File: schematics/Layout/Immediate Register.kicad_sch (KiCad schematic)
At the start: 3 parts

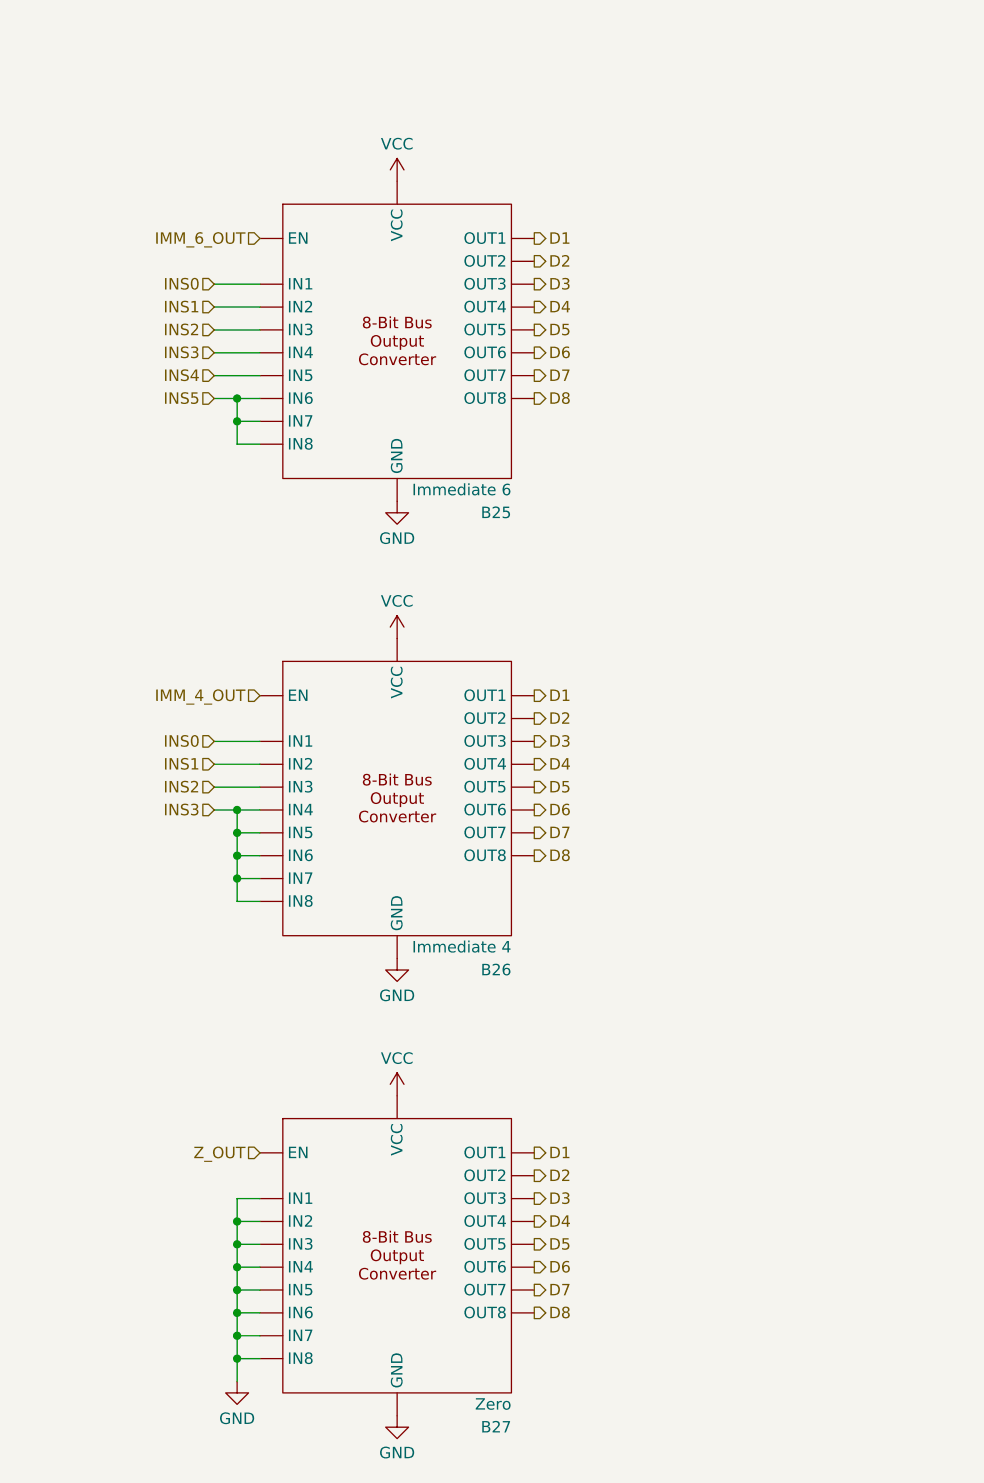
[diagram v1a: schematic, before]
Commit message: Update layout diagram with new boards in following places:  - Added buffer boards to all register boards.  - Fixed PC not getting address lines.  - Added SRAM interface boards.  - Updated to use Mini Control Signals Distributors.
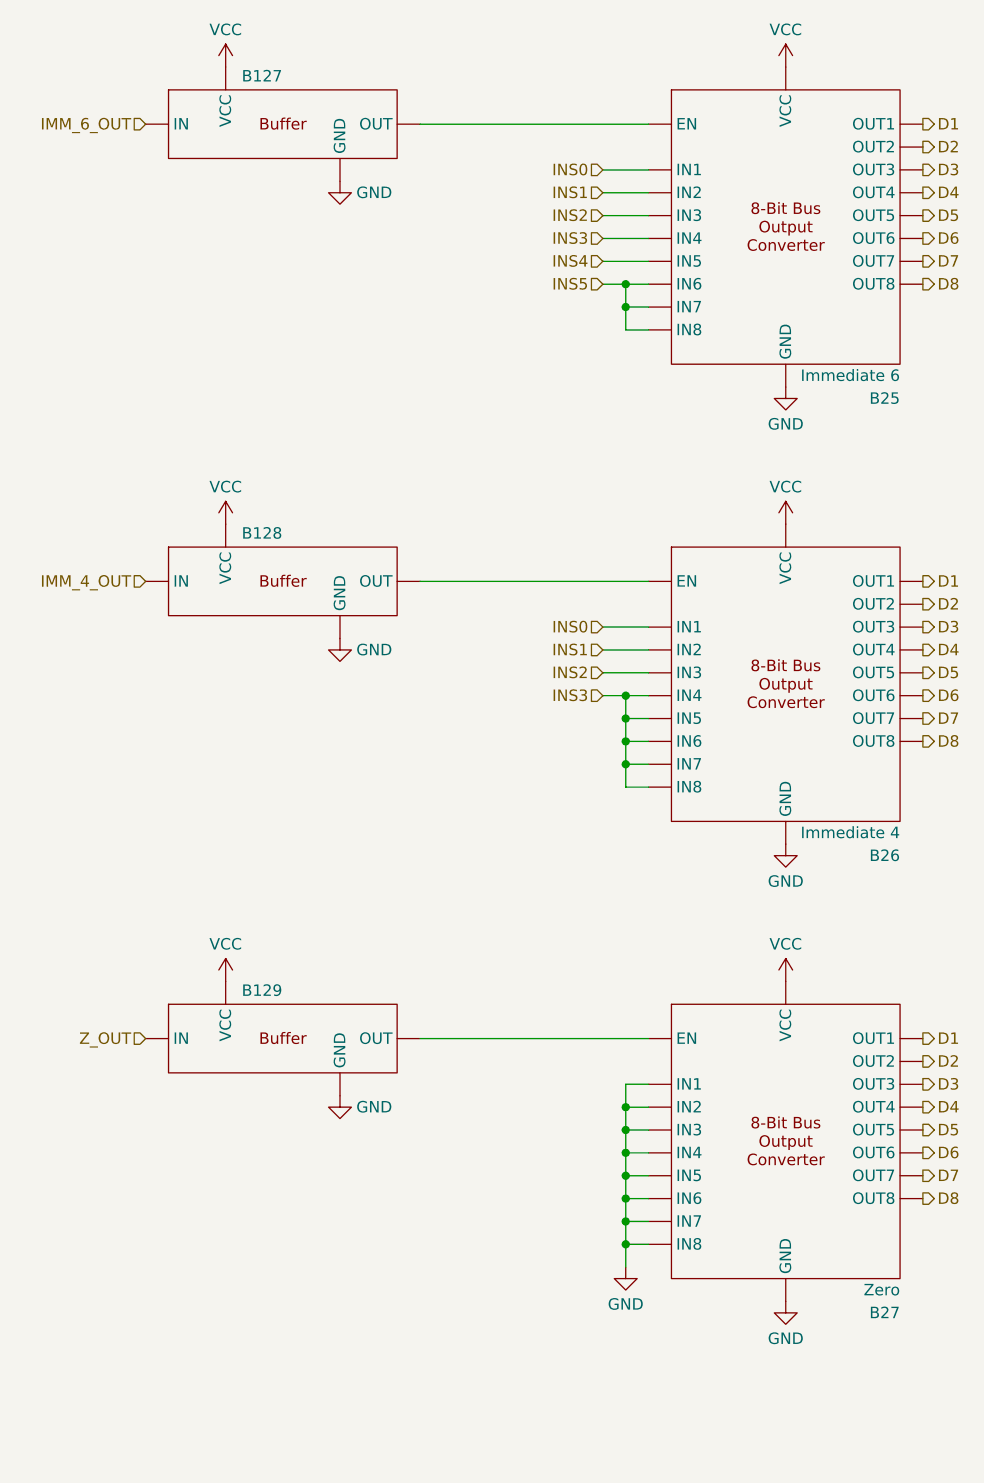
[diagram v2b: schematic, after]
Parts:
- added B127, B128, B129: ~, symbol MiniDragon:Logic Buffer
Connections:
- net GND: now also B127. (OUT), B128. (OUT), B129. (OUT)
- net IMM_4_OUT: now also B128. (OUT); no longer B26. (OUT8)
- net IMM_6_OUT: now also B127. (OUT); no longer B25. (OUT8)
- net VCC: now also B127. (OUT), B128. (OUT), B129. (OUT)
- net Z_OUT: now also B129. (OUT); no longer B27. (OUT8)
- new net: B129. (OUT), B27. (OUT8)
- new net: B127. (OUT), B25. (OUT8)
- new net: B128. (OUT), B26. (OUT8)
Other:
- moved on the sheet: B25, B26, B27

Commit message: Update with new Shift symbol, diagram the rest of the ALU and more instruction decoder boards.
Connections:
- new net: B129. (OUT), B27. (OUT8)
- new net: B127. (OUT), B25. (OUT8)
- new net: B128. (OUT), B26. (OUT8)
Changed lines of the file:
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@@
 	)
 	(symbol
-		(lib_name "Logic Buffer_2")
 		(lib_id "MiniDragon:Logic Buffer")
 		(at 76.2 143.51 0)
@@
 	)
 	(symbol
+		(lib_name "8-bit Bus Output_2")
+		(lib_id "MiniDragon:8-bit Bus Output")
+		(at 132.08 53.34 0)
+		(unit 1)
+		(exclude_from_sim no)
+		(in_bom yes)
+		(on_board yes)
+		(dnp no)
+		(property "Reference" "B25"
+			(at 144.78 72.39 0)
+			(effects
+				(font
+					(size 1.27 1.27)
+				)
+				(justify right)
+			)
+		)
+		(property "Value" "Immediate 6"
+			(at 144.78 69.85 0)
+			(effects
+				(font
+					(size 1.27 1.27)
+				)
+				(justify right)
+			)
+		)
+		(property "Footprint" ""
+			(at 132.08 50.8 0)
+			(effects
+				(font
+					(size 1.27 1.27)
+				)
+				(hide yes)
+			)
+		)
+		(property "Datasheet" ""
+			(at 132.08 50.8 0)
+			(effects
+				(font
+					(size 1.27 1.27)
+				)
+				(hide yes)
+			)
+		)
+		(property "Description" ""
+			(at 132.08 53.34 0)
+			(effects
+				(font
+					(size 1.27 1.27)
+				)
+			)
+		)
+		(pin ""
+		)
+		(pin ""
+		)
+		(pin ""
+		)
+		(pin ""
+		)
+		(pin ""
+		)
+		(pin ""
+		)
+		(pin ""
+		)
+		(pin ""
+		)
+		(pin ""
+		)
+		(pin ""
+		)
+		(pin ""
+		)
+		(pin ""
+		)
+		(pin ""
+		)
+		(pin ""
+		)
+		(pin ""
+		)
+		(pin ""
+		)
+		(pin ""
+		)
+		(pin ""
+		)
+		(pin ""
+		)
+		(instances
+			(project "MiniDragon"
+				(path "/5049efcd-4f75-45d1-9c4f-a0a8d8f08d5b/22b03389-15d6-4e58-ab5f-e64946b54731"
+					(reference "B25")
+					(unit 1)
+				)
+			)
+		)
+	)
+	(symbol
+		(lib_name "Logic Buffer_2")
+		(lib_id "MiniDragon:Logic Buffer")
+		(at 76.2 41.91 0)
+		(unit 1)
+		(exclude_from_sim no)
+		(in_bom yes)
+		(on_board yes)
+		(dnp no)
+		(property "Reference" "B127"
+			(at 71.628 36.576 0)
+			(effects
+				(font
+					(size 1.27 1.27)
+				)
+				(justify left)
+			)
+		)
+		(property "Value" "~"
+			(at 71.9933 36.5068 0)
+			(effects
+				(font
+					(size 1.27 1.27)
+				)
+				(justify left)
+				(hide yes)
+			)
+		)
+		(property "Footprint" ""
+			(at 76.2 50.8 0)
+			(effects
+				(font
+					(size 1.27 1.27)
+				)
+				(hide yes)
+			)
+		)
+		(property "Datasheet" ""
+			(at 76.2 50.8 0)
+			(effects
+				(font
+					(size 1.27 1.27)
+				)
+				(hide yes)
+			)
+		)
+		(property "Description" ""
+			(at 76.2 41.91 0)
+			(effects
+				(font
+					(size 1.27 1.27)
+				)
+				(hide yes)
+			)
+		)
+		(pin ""
+		)
+		(pin ""
+		)
+		(pin ""
+		)
+		(pin ""
+		)
+		(instances
+			(project "MiniDragon"
+				(path "/5049efcd-4f75-45d1-9c4f-a0a8d8f08d5b/22b03389-15d6-4e58-ab5f-e64946b54731"
+					(reference "B127")
+					(unit 1)
+				)
+			)
+		)
+	)
+	(symbol
+		(lib_id "power:GND")
+		(at 82.55 99.06 0)
+		(unit 1)
+		(exclude_from_sim no)
+		(in_bom yes)
+		(on_board yes)
+		(dnp no)
+		(property "Reference" "#PWR0263"
+			(at 82.55 105.41 0)
+			(effects
+				(font
+					(size 1.27 1.27)
+				)
+				(hide yes)
+			)
+		)
+		(property "Value" "GND"
+			(at 86.36 100.33 0)
+			(effects
+				(font
+					(size 1.27 1.27)
+				)
+			)
+		)
+		(property "Footprint" ""
+			(at 82.55 99.06 0)
+			(effects
+				(font
+					(size 1.27 1.27)
+				)
+				(hide yes)
+			)
+		)
+		(property "Datasheet" ""
+			(at 82.55 99.06 0)
+			(effects
+				(font
+					(size 1.27 1.27)
+				)
+				(hide yes)
+			)
+		)
+		(property "Description" ""
+			(at 82.55 99.06 0)
+			(effects
+				(font
+					(size 1.27 1.27)
+				)
+			)
+		)
+		(pin "1"
+		)
+		(instances
+			(project "MiniDragon"
+				(path "/5049efcd-4f75-45d1-9c4f-a0a8d8f08d5b/22b03389-15d6-4e58-ab5f-e64946b54731"
+					(reference "#PWR0263")
+					(unit 1)
+				)
+			)
+		)
+	)
+	(symbol
 		(lib_name "8-bit Bus Output_1")
 		(lib_id "MiniDragon:8-bit Bus Output")
-		(at 132.08 53.34 0)
-		(unit 1)
-		(exclude_from_sim no)
-		(in_bom yes)
-		(on_board yes)
-		(dnp no)
-		(property "Reference" "B25"
-			(at 144.78 72.39 0)
-			(effects
-				(font
-					(size 1.27 1.27)
-				)
-				(justify right)
-			)
-		)
-		(property "Value" "Immediate 6"
-			(at 144.78 69.85 0)
-			(effects
-				(font
-					(size 1.27 1.27)
-				)
-				(justify right)
-			)
-		)
-		(property "Footprint" ""
-			(at 132.08 50.8 0)
-			(effects
-				(font
-					(size 1.27 1.27)
-				)
-				(hide yes)
-			)
-		)
-		(property "Datasheet" ""
-			(at 132.08 50.8 0)
-			(effects
-				(font
-					(size 1.27 1.27)
-				)
-				(hide yes)
-			)
-		)
-		(property "Description" ""
-			(at 132.08 53.34 0)
-			(effects
-				(font
-					(size 1.27 1.27)
-				)
-			)
-		)
-		(pin ""
-		)
-		(pin ""
-		)
-		(pin ""
-		)
-		(pin ""
-		)
-		(pin ""
-		)
-		(pin ""
-		)
-		(pin ""
-		)
-		(pin ""
-		)
-		(pin ""
-		)
-		(pin ""
-		)
-		(pin ""
-		)
-		(pin ""
-		)
-		(pin ""
-		)
-		(pin ""
-		)
-		(pin ""
-		)
-		(pin ""
-		)
-		(pin ""
-		)
-		(pin ""
-		)
-		(pin ""
-		)
-		(instances
-			(project "MiniDragon"
-				(path "/5049efcd-4f75-45d1-9c4f-a0a8d8f08d5b/22b03389-15d6-4e58-ab5f-e64946b54731"
-					(reference "B25")
-					(unit 1)
-				)
-			)
-		)
-	)
-	(symbol
-		(lib_id "MiniDragon:Logic Buffer")
-		(at 76.2 41.91 0)
-		(unit 1)
-		(exclude_from_sim no)
-		(in_bom yes)
-		(on_board yes)
-		(dnp no)
-		(property "Reference" "B127"
-			(at 71.628 36.576 0)
-			(effects
-				(font
-					(size 1.27 1.27)
-				)
-				(justify left)
-			)
-		)
-		(property "Value" "~"
-			(at 71.9933 36.5068 0)
-			(effects
-				(font
-					(size 1.27 1.27)
-				)
-				(justify left)
-				(hide yes)
-			)
-		)
-		(property "Footprint" ""
-			(at 76.2 50.8 0)
-			(effects
-				(font
-					(size 1.27 1.27)
-				)
-				(hide yes)
-			)
-		)
-		(property "Datasheet" ""
-			(at 76.2 50.8 0)
-			(effects
-				(font
-					(size 1.27 1.27)
-				)
-				(hide yes)
-			)
-		)
-		(property "Description" ""
-			(at 76.2 41.91 0)
-			(effects
-				(font
-					(size 1.27 1.27)
-				)
-				(hide yes)
-			)
-		)
-		(pin ""
-		)
-		(pin ""
-		)
-		(pin ""
-		)
-		(pin ""
-		)
-		(instances
-			(project "MiniDragon"
-				(path "/5049efcd-4f75-45d1-9c4f-a0a8d8f08d5b/22b03389-15d6-4e58-ab5f-e64946b54731"
-					(reference "B127")
-					(unit 1)
-				)
-			)
-		)
-	)
-	(symbol
-		(lib_id "power:GND")
-		(at 82.55 99.06 0)
-		(unit 1)
-		(exclude_from_sim no)
-		(in_bom yes)
-		(on_board yes)
-		(dnp no)
-		(property "Reference" "#PWR0263"
-			(at 82.55 105.41 0)
-			(effects
-				(font
-					(size 1.27 1.27)
-				)
-				(hide yes)
-			)
-		)
-		(property "Value" "GND"
-			(at 86.36 100.33 0)
-			(effects
-				(font
-					(size 1.27 1.27)
-				)
-			)
-		)
-		(property "Footprint" ""
-			(at 82.55 99.06 0)
-			(effects
-				(font
-					(size 1.27 1.27)
-				)
-				(hide yes)
-			)
-		)
-		(property "Datasheet" ""
-			(at 82.55 99.06 0)
-			(effects
-				(font
-					(size 1.27 1.27)
-				)
-				(hide yes)
-			)
-		)
-		(property "Description" ""
-			(at 82.55 99.06 0)
-			(effects
-				(font
-					(size 1.27 1.27)
-				)
-			)
-		)
-		(pin "1"
-		)
-		(instances
-			(project "MiniDragon"
-				(path "/5049efcd-4f75-45d1-9c4f-a0a8d8f08d5b/22b03389-15d6-4e58-ab5f-e64946b54731"
-					(reference "#PWR0263")
-					(unit 1)
-				)
-			)
-		)
-	)
-	(symbol
-		(lib_name "8-bit Bus Output_2")
-		(lib_id "MiniDragon:8-bit Bus Output")
 		(at 132.08 104.14 0)
